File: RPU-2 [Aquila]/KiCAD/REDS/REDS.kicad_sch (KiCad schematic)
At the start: 7 parts, among them M1 Motor_Servo, U1 TLP3545, U2 TLP3545, U3 LM555xN

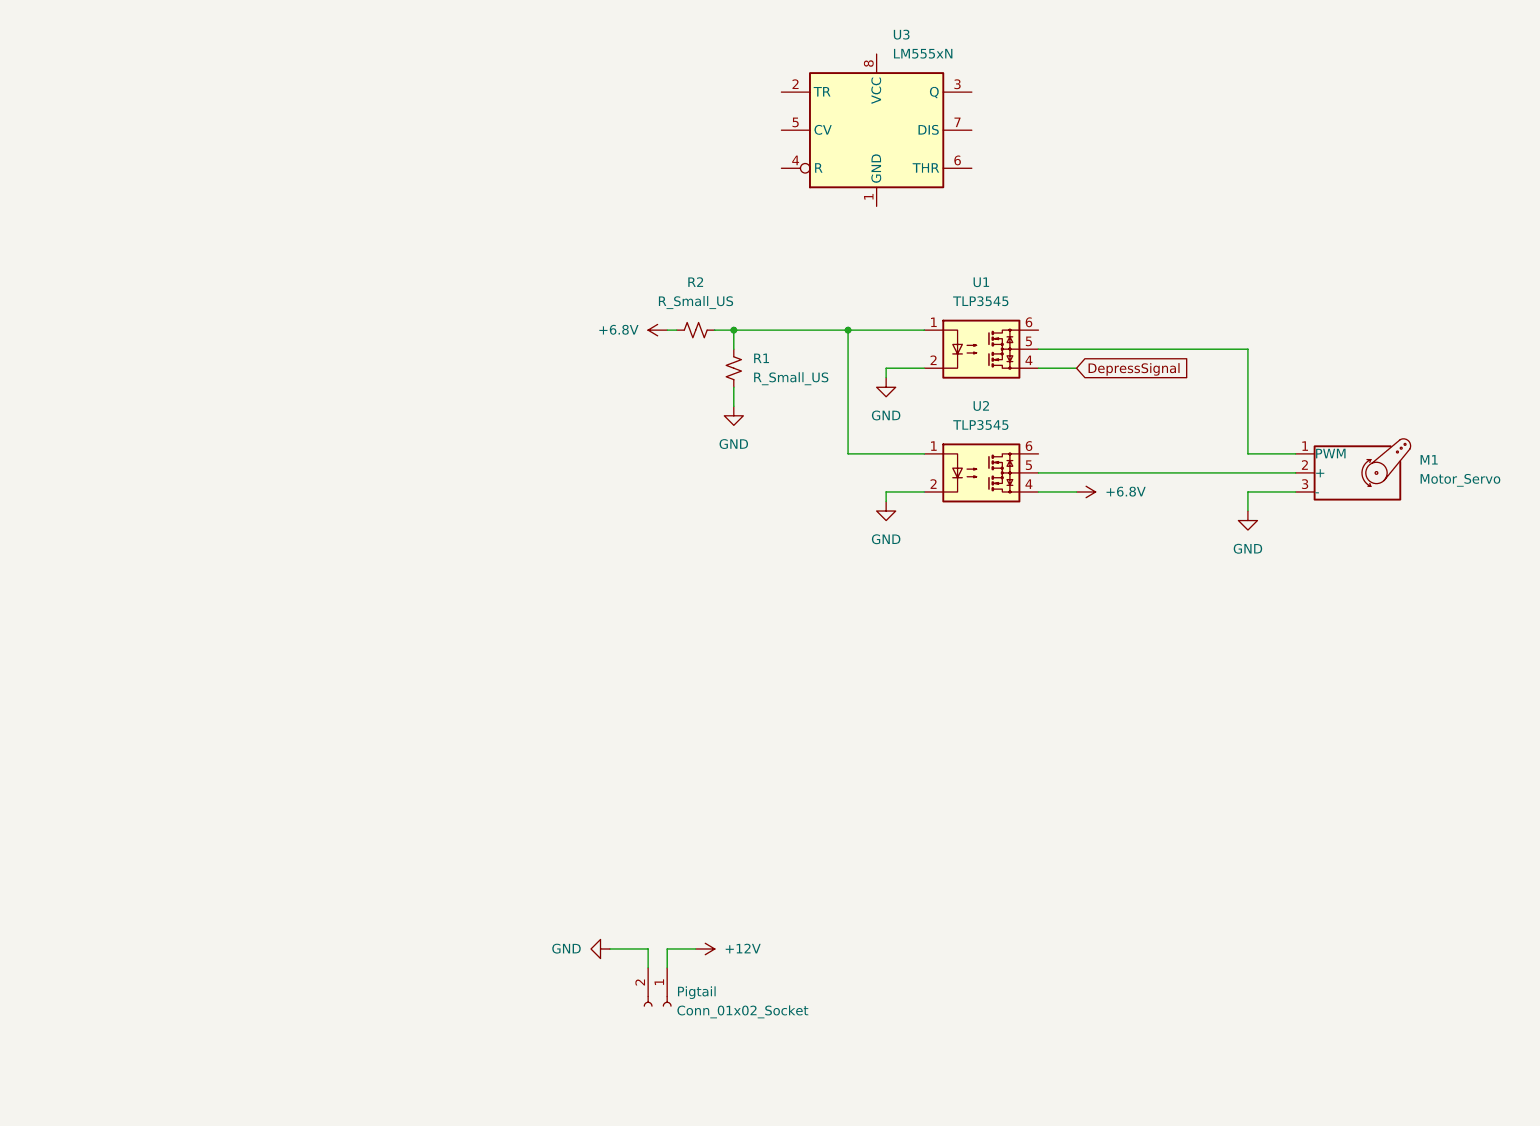
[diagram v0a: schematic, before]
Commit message: Updated Switching Circuit
Designed a switching circuit to use diodes for power switching and a MAX4543 for pwm switching.
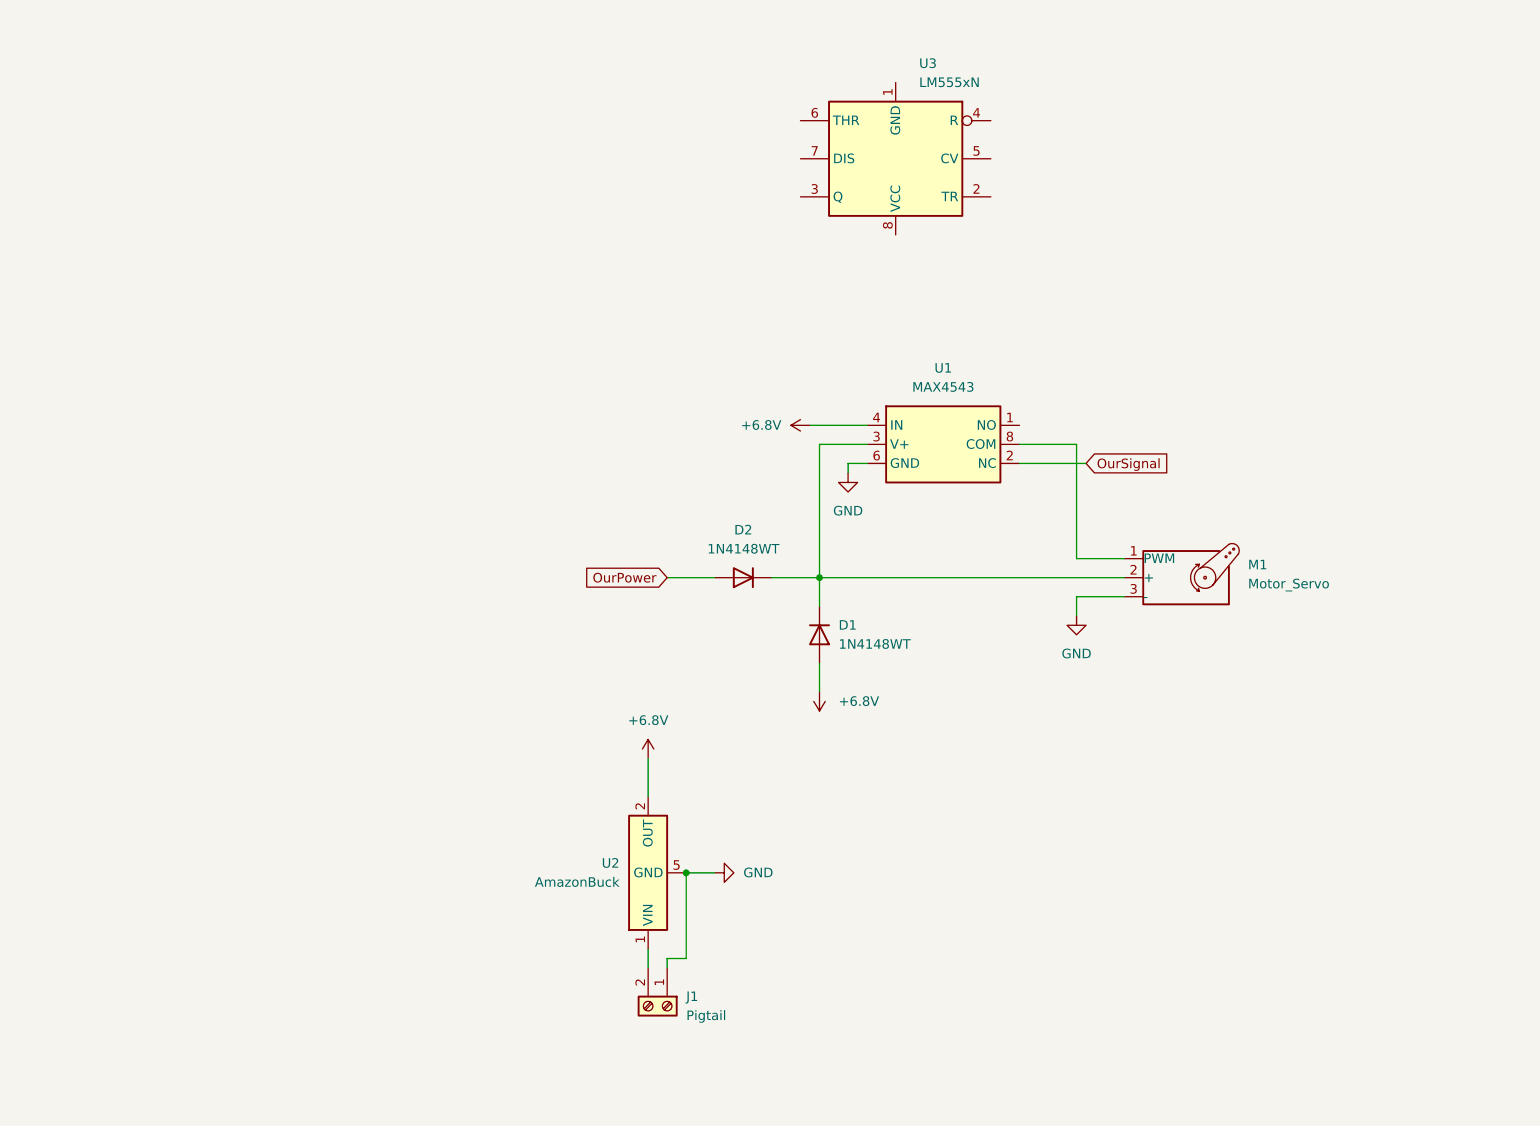
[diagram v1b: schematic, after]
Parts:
- removed Pigtail: Conn_01x02_Socket, symbol Connector:Conn_01x02_Socket
- removed R1, R2: R_Small_US, symbol Device:R_Small_US
- removed U1, U2: TLP3545, Package_DIP:DIP-6_W7.62mm, symbol Relay_SolidState:TLP3545
- added D1, D2: 1N4148WT, Diode_SMD:D_SOD-523, symbol Diode:1N4148WT
- added J1: Pigtail, symbol Connector:Screw_Terminal_01x02
- added U1: MAX4543, Package_SO:MSOP-8_3x3mm_P0.65mm, symbol MAX4543:MAX4543
- added U2: AmazonBuck, Package_SO:SOIC-8_3.9x4.9mm_P1.27mm, symbol AmazonBuck:AmazonBuck
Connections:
- net +6.8V: now also D1.2 (A), U1.4 (IN), U2.2 (OUT)
- net GND: now also J1.1 (Pin_1), U1.6 (GND), U2.5 (GND), U2.6 (GND), U2.7 (GND), U2.8 (GND)
- net at M1.1 (PWM): now also U1.8 (COM)
- net at M1.2 (+): now also D1.1 (K), D2.1 (K), U1.3 (V+)
- new net: J1.2 (Pin_2), U2.1 (VIN)
- new net OurPower: D2.2 (A)
- new net OurSignal: U1.2 (NC)
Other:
- moved on the sheet: M1, U3

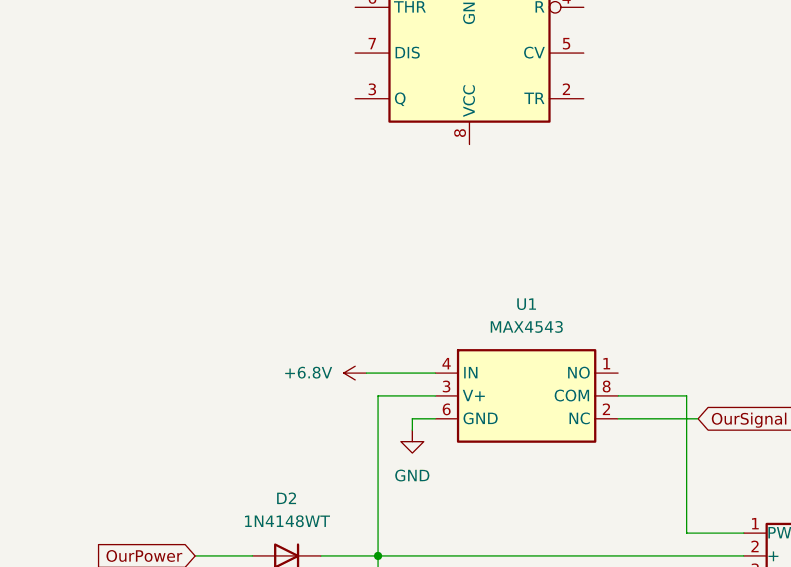
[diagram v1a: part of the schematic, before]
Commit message: Added pull down
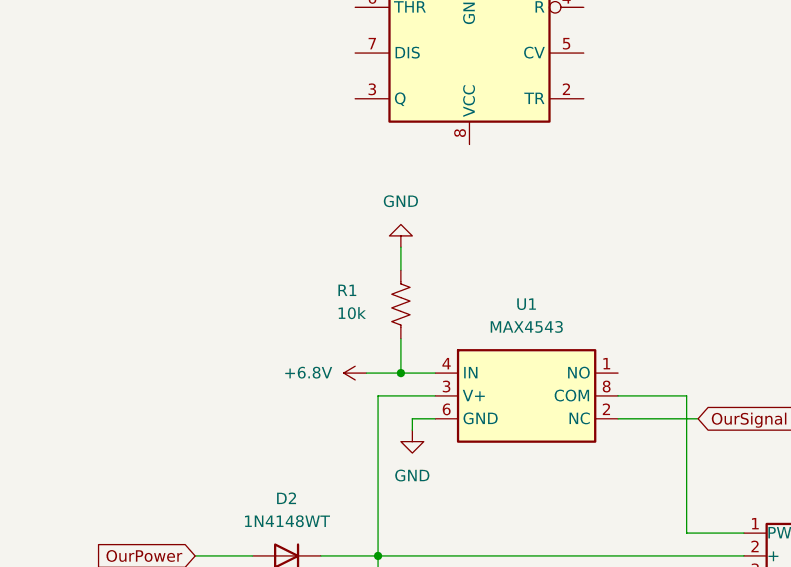
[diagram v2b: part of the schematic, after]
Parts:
- added R1: 10k, symbol Device:R_US
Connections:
- net +6.8V: now also R1.1
- net GND: now also R1.2
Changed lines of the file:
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@@
 		(color 0 0 0 0)
 	)
+	(junction
+		(at 133.35 76.2)
+		(diameter 0)
+		(color 0 0 0 0)
+	)
 	(wire
 		(pts
@@
 	(wire
 		(pts
-			(xy 129.54 76.2) (xy 137.16 76.2)
+			(xy 129.54 76.2) (xy 133.35 76.2)
+		)
+		(stroke
+			(width 0)
+			(type default)
+		)
+	)
+	(wire
+		(pts
+			(xy 133.35 62.23) (xy 133.35 64.77)
 		)
 		(stroke
@@
 	(wire
 		(pts
+			(xy 133.35 72.39) (xy 133.35 76.2)
+		)
+		(stroke
+			(width 0)
+			(type default)
+		)
+	)
+	(wire
+		(pts
 			(xy 157.48 78.74) (xy 165.1 78.74)
+		)
+		(stroke
+			(width 0)
+			(type default)
+		)
+	)
+	(wire
+		(pts
+			(xy 133.35 76.2) (xy 137.16 76.2)
 		)
 		(stroke
@@
 	)
 	(symbol
+		(lib_id "power:GND")
+		(at 133.35 62.23 180)
+		(unit 1)
+		(exclude_from_sim no)
+		(in_bom yes)
+		(on_board yes)
+		(dnp no)
+		(fields_autoplaced yes)
+		(property "Reference" "#PWR05"
+			(at 133.35 55.88 0)
+			(effects
+				(font
+					(size 1.27 1.27)
+				)
+				(hide yes)
+			)
+		)
+		(property "Value" "GND"
+			(at 133.35 57.15 0)
+			(effects
+				(font
+					(size 1.27 1.27)
+				)
+			)
+		)
+		(property "Footprint" ""
+			(at 133.35 62.23 0)
+			(effects
+				(font
+					(size 1.27 1.27)
+				)
+				(hide yes)
+			)
+		)
+		(property "Datasheet" ""
+			(at 133.35 62.23 0)
+			(effects
+				(font
+					(size 1.27 1.27)
+				)
+				(hide yes)
+			)
+		)
+		(property "Description" "Power symbol creates a global label with name \"GND\" , ground"
+			(at 133.35 62.23 0)
+			(effects
+				(font
+					(size 1.27 1.27)
+				)
+				(hide yes)
+			)
+		)
+		(pin "1"
+		)
+		(instances
+			(project "REDS"
+				(path "/b41176b4-ee35-4242-bb55-a96abde584dd"
+					(reference "#PWR05")
+					(unit 1)
+				)
+			)
+		)
+	)
+	(symbol
 		(lib_id "Diode:1N4148WT")
 		(at 130.81 104.14 270)
@@
 					(unit 1)
 				)
+			)
+		)
+	)
+	(symbol
+		(lib_id "Device:R_US")
+		(at 133.35 68.58 180)
+		(unit 1)
+		(exclude_from_sim no)
+		(in_bom yes)
+		(on_board yes)
+		(dnp no)
+		(property "Reference" "R1"
+			(at 126.238 67.056 0)
+			(effects
+				(font
+					(size 1.27 1.27)
+				)
+				(justify right)
+			)
+		)
+		(property "Value" "10k"
+			(at 126.238 69.596 0)
+			(effects
+				(font
+					(size 1.27 1.27)
+				)
+				(justify right)
+			)
+		)
+		(property "Footprint" ""
+			(at 132.334 68.326 90)
+			(effects
+				(font
+					(size 1.27 1.27)
+				)
+				(hide yes)
+			)
+		)
+		(property "Datasheet" "~"
+			(at 133.35 68.58 0)
+			(effects
+				(font
+					(size 1.27 1.27)
+				)
+				(hide yes)
+			)
+		)
+		(property "Description" "Resistor, US symbol"
+			(at 133.35 68.58 0)
+			(effects
+				(font
+					(size 1.27 1.27)
+				)
+				(hide yes)
+			)
+		)
+		(pin "2"
+		)
+		(pin "1"
+		)
+		(instances
+			(project ""
+				(path "/b41176b4-ee35-4242-bb55-a96abde584dd"
+					(reference "R1")
+					(unit 1)
+				)

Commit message: Started 555
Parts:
- added 100nF, 1nF: C_Small, symbol Device:C_Small
- added R2: R_US, symbol Device:R_US
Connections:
- net +6.8V: now also U3.4 (R), U3.8 (VCC), R2.1
- net GND: now also U3.1 (GND), 100nF.2, 1nF.2
- net at U3.2 (TR): now also U3.6 (THR), 100nF.1
- net at U3.5 (CV): now also 1nF.1
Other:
- moved on the sheet: D1, D2, J1, M1, R1, U1, U2, U3

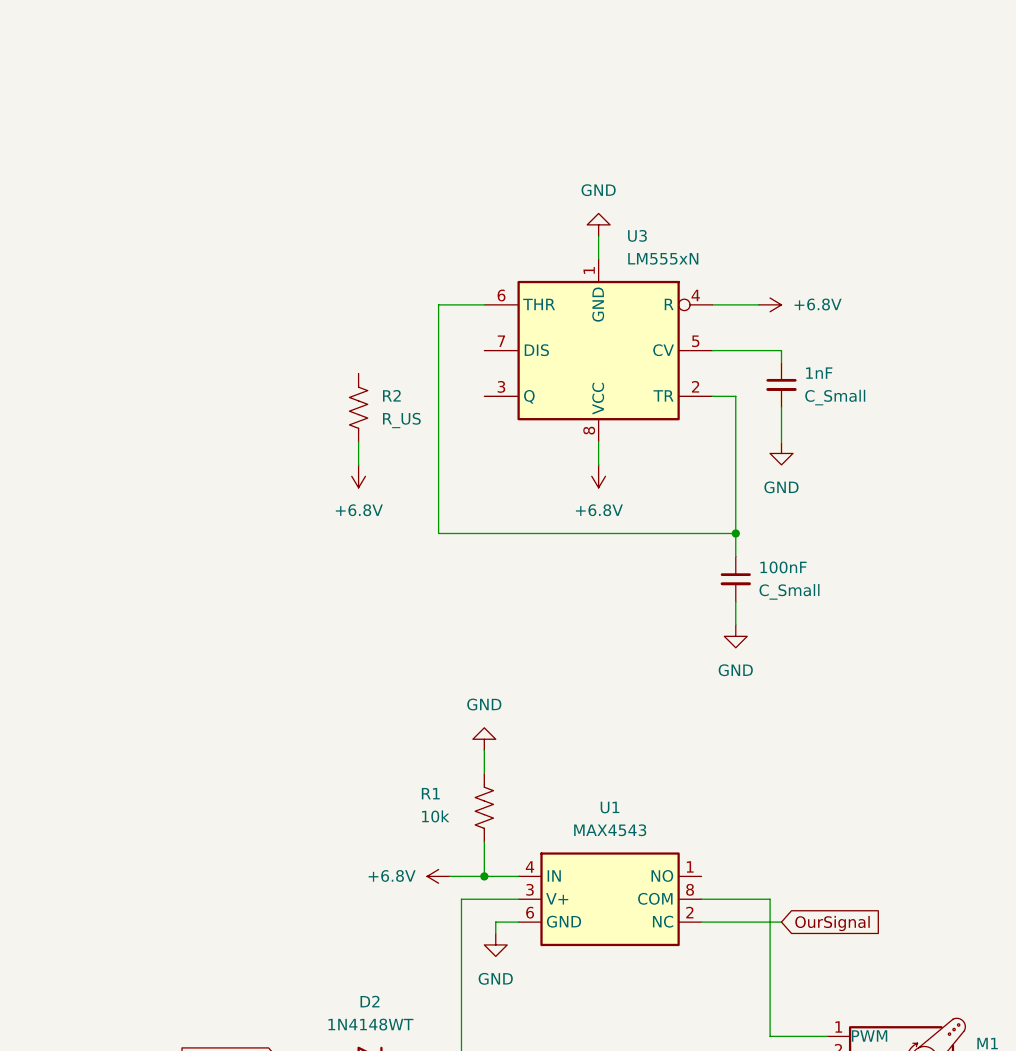
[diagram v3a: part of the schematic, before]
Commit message: schematic done and update to kicad 10.0
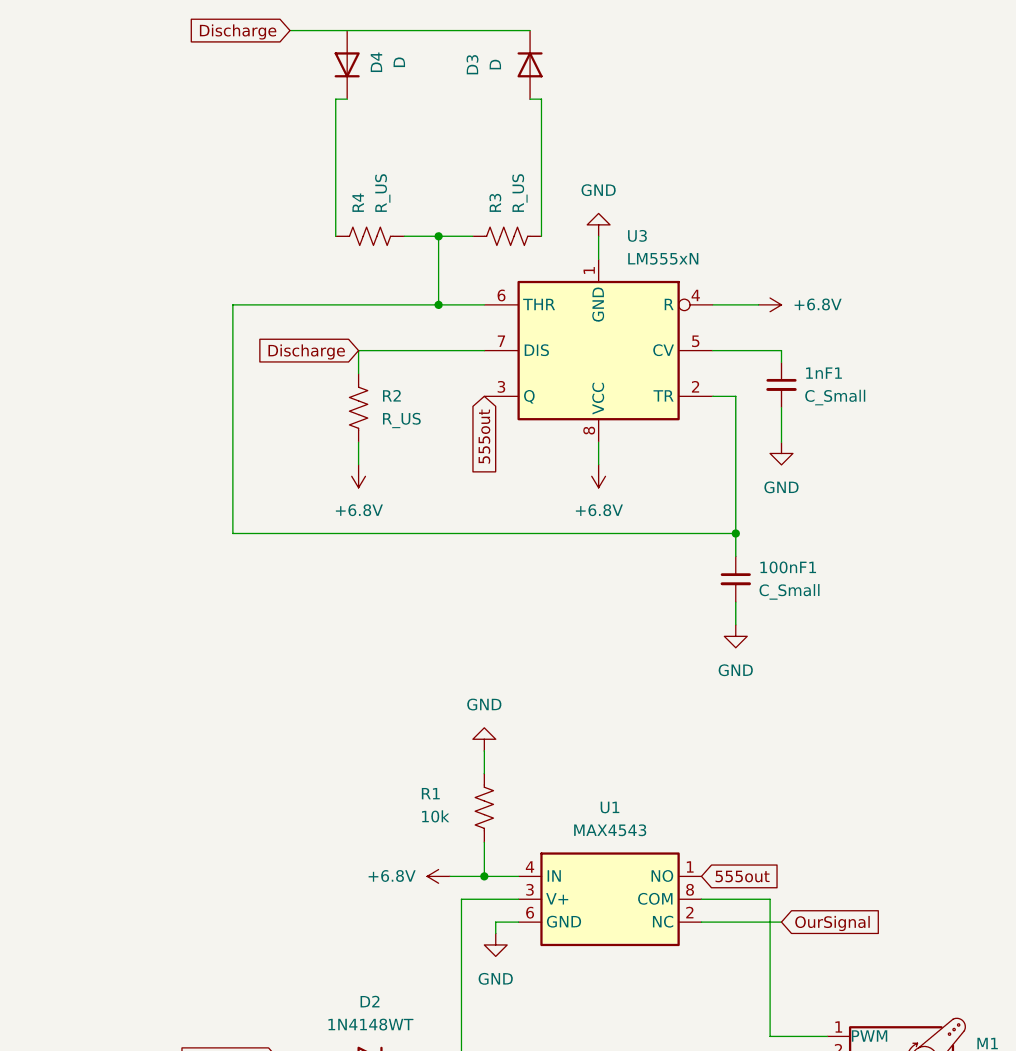
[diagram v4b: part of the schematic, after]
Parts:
- added D3, D4: D, symbol Device:D
- added R3, R4: R_US, symbol Device:R_US
- renumbered 100nF to 100nF1, 1nF to 1nF1
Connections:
- net at 100nF1.1, U3.2 (TR), U3.6 (THR): now also R3.1, R4.2
- net 555out: now reaches U3.3 (Q)
- net 555out: now also U1.1 (NO)
- net Discharge: now reaches U3.7 (DIS)
- net Discharge: now also R2.2, D3.1 (K)
- new net: D4.1 (K), R4.1
- new net: D3.2 (A), R3.2

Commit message: 555 change
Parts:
- removed D4: D, symbol Device:D
- removed R3: R_US, symbol Device:R_US
- 100nF1, 1nF1: footprint (none) -> Capacitor_THT:CP_Radial_D5.0mm_P2.50mm
- D3: footprint (none) -> Diode_THT:D_DO-201_P15.24mm_Horizontal
- J1: footprint (none) -> TerminalBlock_WAGO:TerminalBlock_WAGO_804-302_1x02_P7.50mm_45Degree
- M1: footprint (none) -> TerminalBlock_WAGO:TerminalBlock_WAGO_804-303_1x03_P7.50mm_45Degree
- R1, R2, R4: footprint (none) -> Resistor_THT:R_Axial_DIN0207_L6.3mm_D2.5mm_P10.16mm_Horizontal
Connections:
- net Discharge: now also D3.2 (A), R4.1; no longer D3.1 (K)
- net at 100nF1.1, R4.2, U3.2 (TR)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: now also D3.1 (K)
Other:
- moved on the sheet: D3, R4
